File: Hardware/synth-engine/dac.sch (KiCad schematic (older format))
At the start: 43 parts, among them U10 NJM4580, U11 NJM4580, U9 AK4490

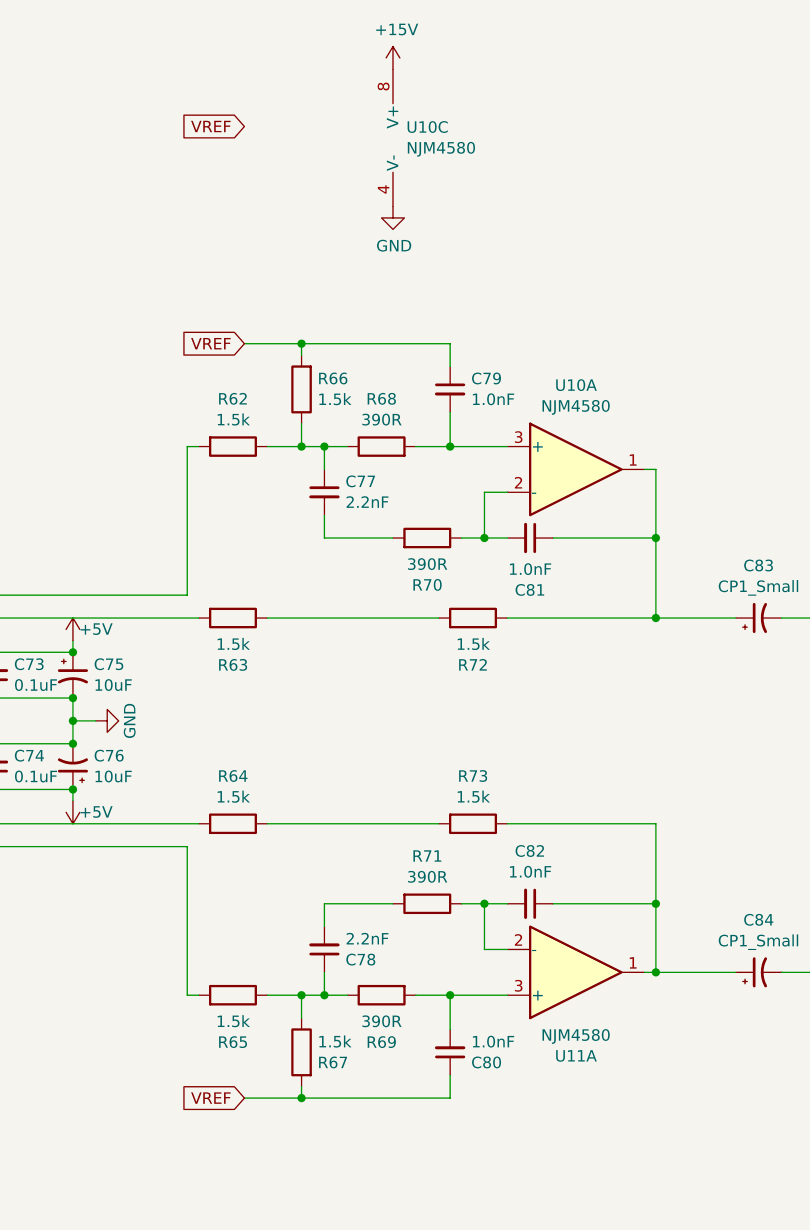
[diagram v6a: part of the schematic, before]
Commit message: rough placement and symbol organization. If I need to start PCB layout over from scracth, revert to this commit.
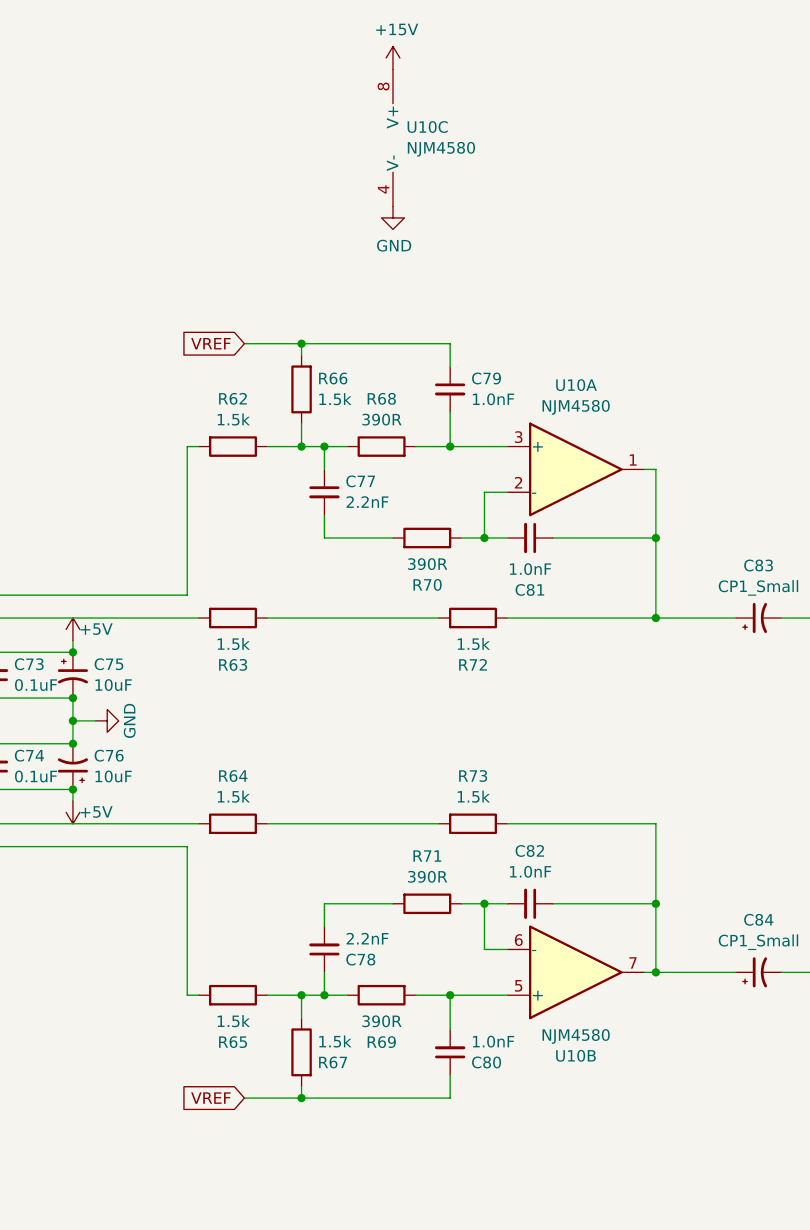
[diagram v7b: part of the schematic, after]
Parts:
- renumbered U11 to U10
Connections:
- net at C82.1, C84.1, R73.1: now also U10.7; no longer U10.1
- net at C82.2, R71.1: now also U10.6 (-); no longer U10.2 (-)
- net at C80.2, R69.2: now also U10.5 (+); no longer U10.3 (+)
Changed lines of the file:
@@
 Text GLabel 6700 2400 0    50   Input ~ 0
-VREF
-Text GLabel 6700 1450 0    50   Input ~ 0
 VREF
 $Comp
@@
 	8450 2950 8500 2950
 Wire Wire Line
-	8500 2950 8500 3250
-Wire Wire Line
-	8500 3250 8050 3250
-Wire Wire Line
 	7850 3600 8500 3600
-Wire Wire Line
-	8500 3600 8500 3250
-Connection ~ 8500 3250
 Wire Wire Line
 	7550 3600 6800 3600
@@
 	5500 3600 6500 3600
 $Comp
-L Amplifier_Operational:NJM4580 U11
-U 1 1 5DE1F686
+L Amplifier_Operational:NJM4580 U10
+U 2 1 5DE1F686
 P 8150 5150
-F 0 "U11" H 8150 5517 50  0000 C CNN
+F 0 "U10" H 8150 5517 50  0000 C CNN
 F 1 "NJM4580" H 8150 5426 50  0000 C CNN
 F 2 "SparkFun-DigitalIC:SO08" H 8150 5150 50  0001 C CNN
 F 3 "http://www.njr.com/semicon/PDF/NJM4580_E.pdf" H 8150 5150 50  0001 C CNN
-	1    8150 5150
+	2    8150 5150
 	1    0    0    1
 $EndComp
@@
 Text Notes 9650 4200 0    50   ~ 0
 I think I  could DC couple this\nand remove coupling caps\nbecause filters will be biased\nto the same VREF (?)
+Wire Wire Line
+	8500 3600 8500 3250
+Wire Wire Line
+	8500 2950 8500 3250
+Connection ~ 8500 3250
+Wire Wire Line
+	8500 3250 8050 3250
 $EndSCHEMATC
